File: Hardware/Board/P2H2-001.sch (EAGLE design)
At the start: 18 parts, among them K1 G5V1, T1 2SC1815

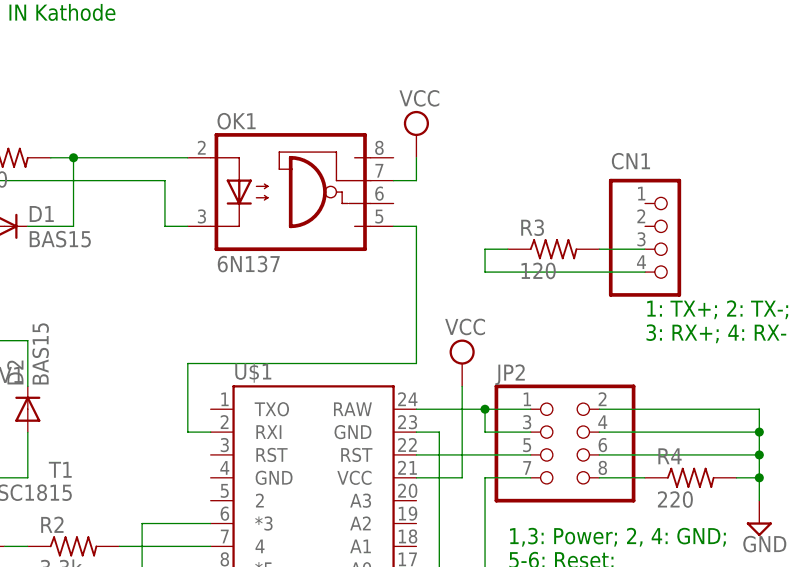
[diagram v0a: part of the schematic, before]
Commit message: Fixed connection error of MIDI IN.
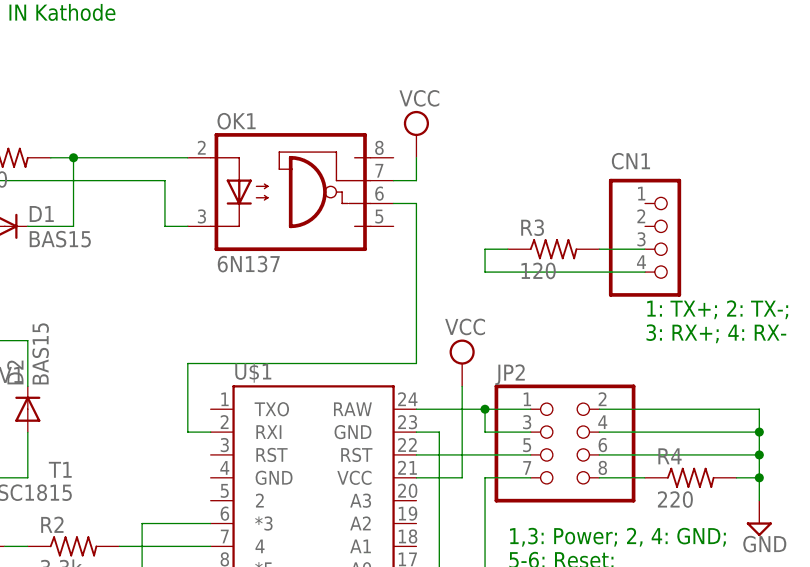
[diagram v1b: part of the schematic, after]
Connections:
- net N$12: now also OK1.VO; no longer OK1.GND
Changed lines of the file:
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@@
 <net name="N$12" class="0">
 <segment>
-<pinref part="OK1" gate="A" pin="GND"/>
-<wire x1="81.28" y1="66.04" x2="83.82" y2="66.04" width="0.1524" layer="91"/>
-<wire x1="83.82" y1="66.04" x2="83.82" y2="50.8" width="0.1524" layer="91"/>
+<wire x1="83.82" y1="68.58" x2="83.82" y2="50.8" width="0.1524" layer="91"/>
 <wire x1="83.82" y1="50.8" x2="58.42" y2="50.8" width="0.1524" layer="91"/>
 <wire x1="58.42" y1="50.8" x2="58.42" y2="43.18" width="0.1524" layer="91"/>
 <pinref part="U$1" gate="G$1" pin="RXI"/>
 <wire x1="58.42" y1="43.18" x2="60.96" y2="43.18" width="0.1524" layer="91"/>
+<pinref part="OK1" gate="A" pin="VO"/>
+<wire x1="81.28" y1="68.58" x2="83.82" y2="68.58" width="0.1524" layer="91"/>
 </segment>
 </net>

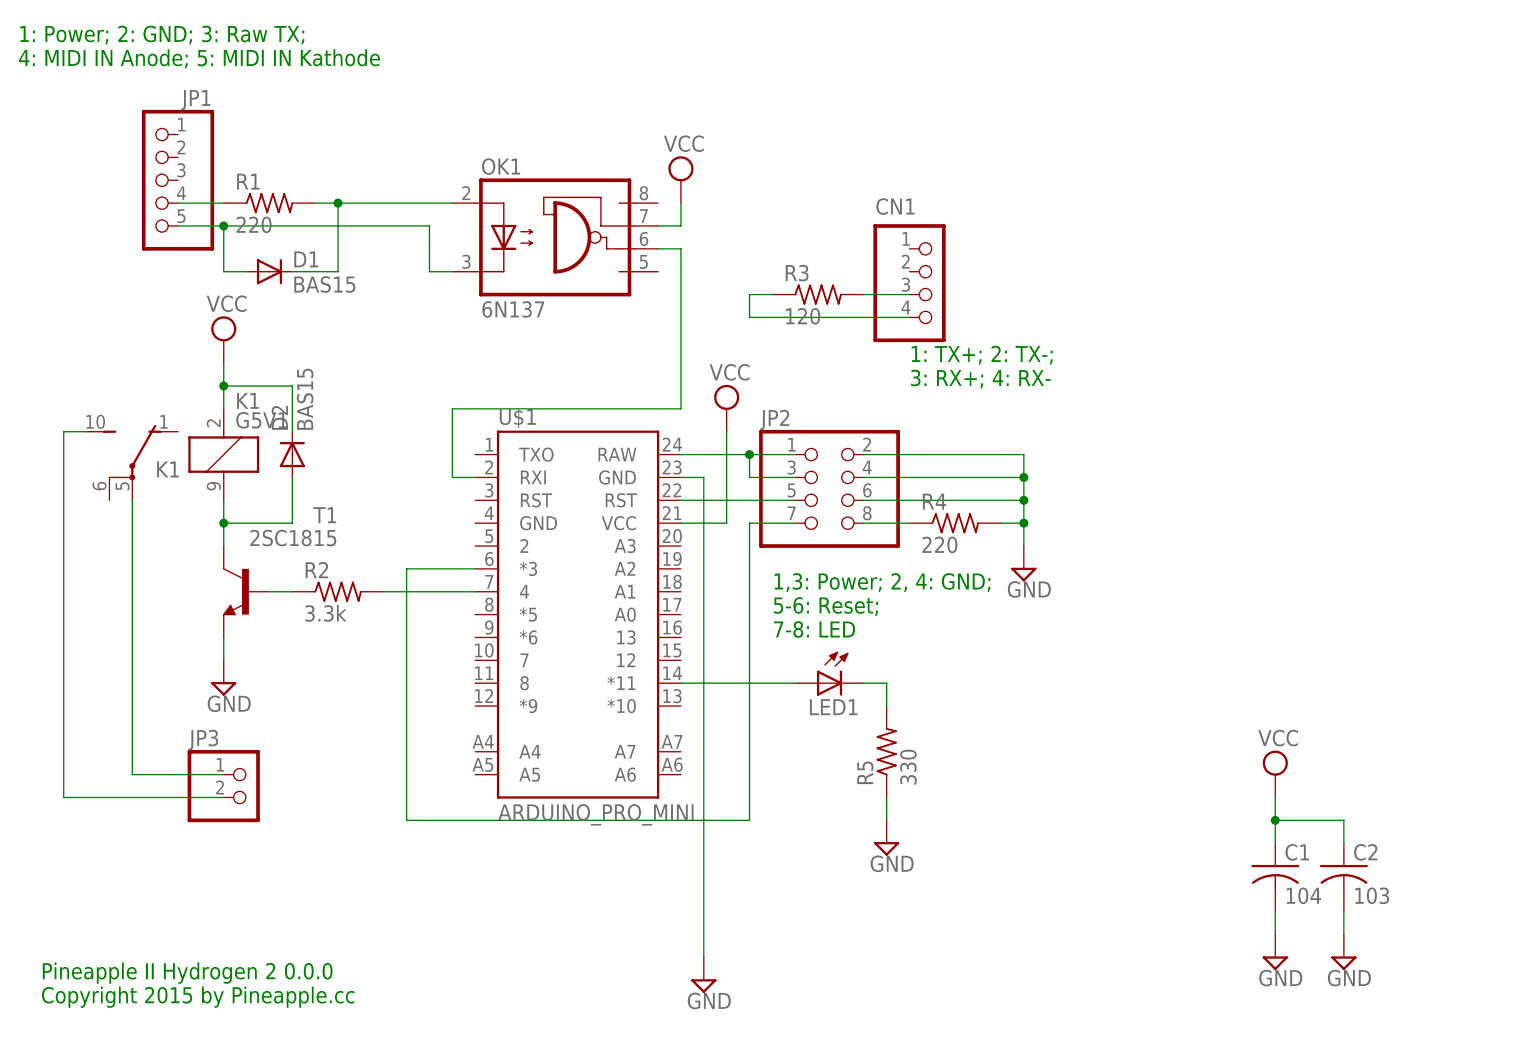
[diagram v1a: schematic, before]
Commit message: Adopted to Relayport.
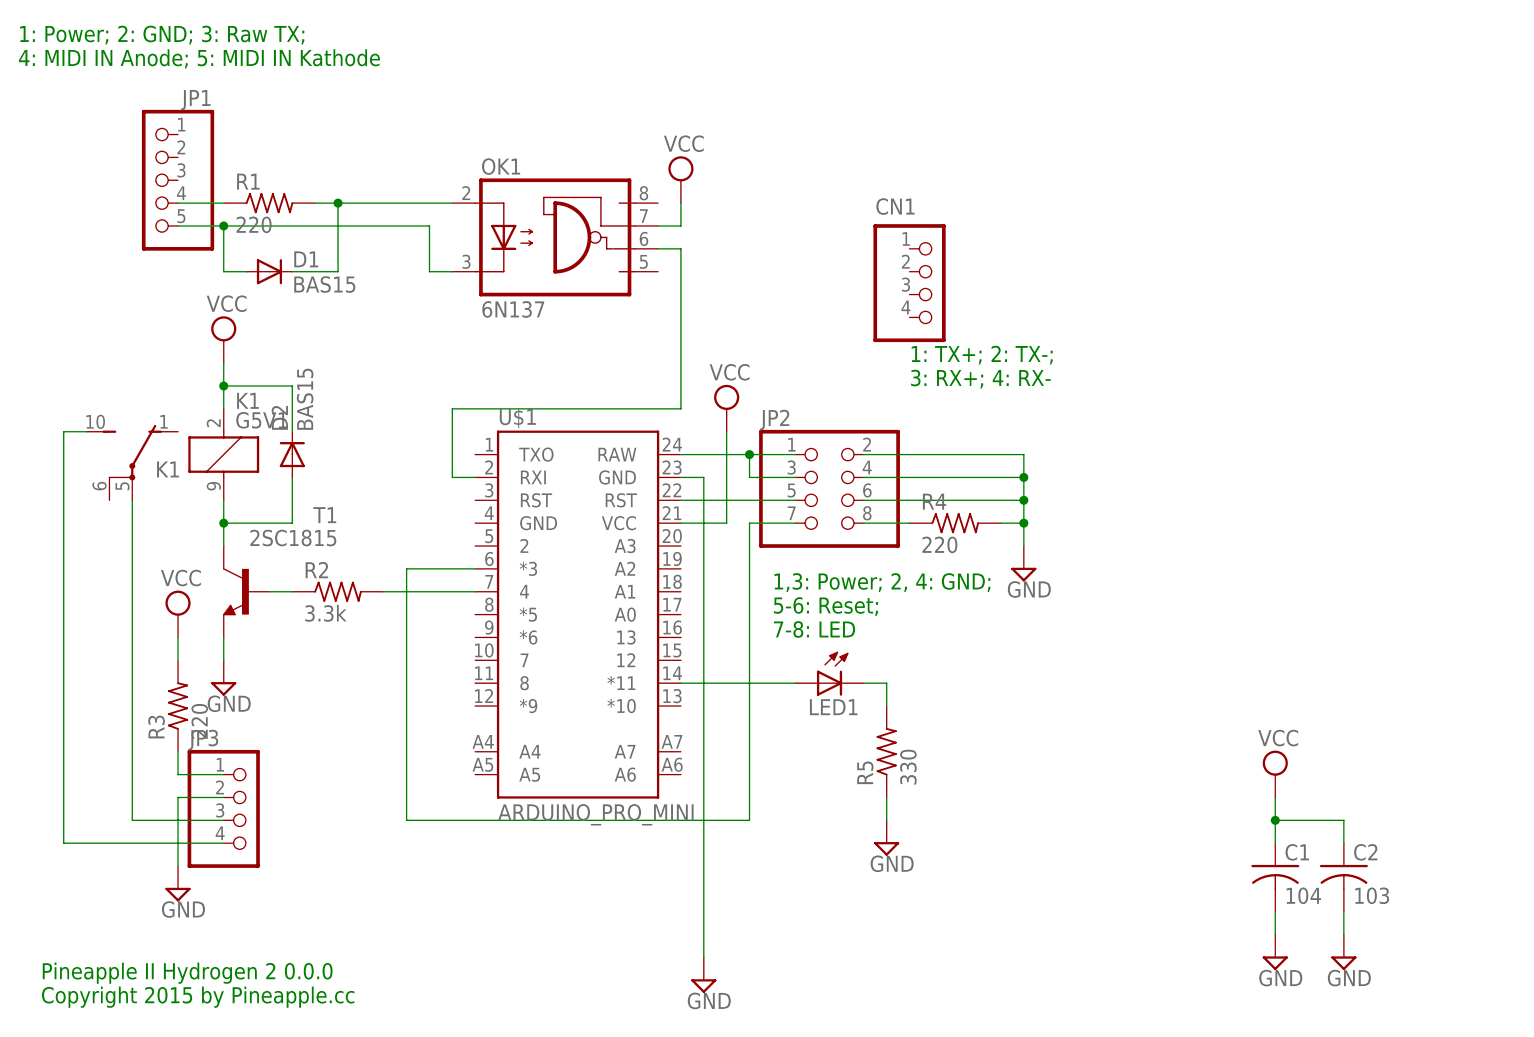
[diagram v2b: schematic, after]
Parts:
- JP3: device pinhead:PINHD-1X2 -> pinhead:PINHD-1X4
- R3: value 120 -> 220
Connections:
- removed net N$1: CN1.3, R3.2
- removed net N$2: CN1.4, R3.1
- new net N$10: JP3.1, R3.1
- net GND: now also JP3.2
- net N$18: now also JP3.3; no longer JP3.1
- net N$19: now also JP3.4; no longer JP3.2
- net VCC: now also R3.2
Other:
- moved on the sheet: R3
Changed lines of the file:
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@@
 <part name="SUPPLY6" library="supply2" deviceset="GND" device=""/>
 <part name="R4" library="resistor" deviceset="R-US_" device="0204/5" value="220"/>
-<part name="R3" library="resistor" deviceset="R-US_" device="0204/5" value="120"/>
+<part name="R3" library="resistor" deviceset="R-US_" device="0204/5" value="220"/>
 <part name="CN1" library="jst-ph" deviceset="B4B-PH-*" device="K-S"/>
 <part name="U$1" library="SparkFun-Boards" deviceset="ARDUINO_PRO_MINI" device=""/>
@@
 <part name="SUPPLY3" library="supply2" deviceset="VCC" device=""/>
 <part name="R2" library="resistor" deviceset="R-US_" device="0204/5" value="3.3k"/>
-<part name="JP3" library="pinhead" deviceset="PINHD-1X2" device=""/>
+<part name="JP3" library="pinhead" deviceset="PINHD-1X4" device=""/>
+<part name="SUPPLY10" library="supply2" deviceset="GND" device=""/>
+<part name="SUPPLY12" library="supply2" deviceset="VCC" device=""/>
 </parts>
 <sheets>
@@
 <instance part="SUPPLY6" gate="GND" x="121.92" y="33.02"/>
 <instance part="R4" gate="G$1" x="114.3" y="38.1"/>
-<instance part="R3" gate="G$1" x="99.06" y="63.5"/>
+<instance part="R3" gate="G$1" x="27.94" y="17.78" rot="R90"/>
 <instance part="CN1" gate="G$1" x="109.22" y="66.04"/>
 <instance part="U$1" gate="G$1" x="71.12" y="30.48"/>
@@
 <instance part="SUPPLY3" gate="G$1" x="33.02" y="58.42"/>
 <instance part="R2" gate="G$1" x="45.72" y="30.48"/>
-<instance part="JP3" gate="G$1" x="35.56" y="7.62"/>
+<instance part="JP3" gate="A" x="35.56" y="5.08"/>
+<instance part="SUPPLY10" gate="GND" x="27.94" y="-2.54"/>
+<instance part="SUPPLY12" gate="G$1" x="27.94" y="27.94"/>
 </instances>
 <busses>
@@
 <wire x1="106.68" y1="5.08" x2="106.68" y2="7.62" width="0.1524" layer="91"/>
 </segment>
+<segment>
+<pinref part="JP3" gate="A" pin="2"/>
+<pinref part="SUPPLY10" gate="GND" pin="GND"/>
+<wire x1="33.02" y1="7.62" x2="27.94" y2="7.62" width="0.1524" layer="91"/>
+<wire x1="27.94" y1="7.62" x2="27.94" y2="0" width="0.1524" layer="91"/>
+</segment>
 </net>
 <net name="VCC" class="0">
@@
 <wire x1="40.64" y1="53.34" x2="33.02" y2="53.34" width="0.1524" layer="91"/>
 <junction x="33.02" y="53.34"/>
+</segment>
+<segment>
+<pinref part="SUPPLY12" gate="G$1" pin="VCC"/>
+<wire x1="27.94" y1="25.4" x2="27.94" y2="22.86" width="0.1524" layer="91"/>
+<pinref part="R3" gate="G$1" pin="2"/>
 </segment>
 </net>
@@
 <segment>
 <pinref part="K1" gate="2" pin="P"/>
-<wire x1="22.86" y1="10.16" x2="22.86" y2="40.64" width="0.1524" layer="91"/>
-<pinref part="JP3" gate="G$1" pin="1"/>
-<wire x1="22.86" y1="10.16" x2="33.02" y2="10.16" width="0.1524" layer="91"/>
+<wire x1="22.86" y1="5.08" x2="22.86" y2="40.64" width="0.1524" layer="91"/>
+<pinref part="JP3" gate="A" pin="3"/>
+<wire x1="33.02" y1="5.08" x2="22.86" y2="5.08" width="0.1524" layer="91"/>
 </segment>
 </net>
@@
 <pinref part="K1" gate="2" pin="S"/>
 <wire x1="17.78" y1="48.26" x2="15.24" y2="48.26" width="0.1524" layer="91"/>
-<wire x1="15.24" y1="48.26" x2="15.24" y2="7.62" width="0.1524" layer="91"/>
-<pinref part="JP3" gate="G$1" pin="2"/>
-<wire x1="15.24" y1="7.62" x2="33.02" y2="7.62" width="0.1524" layer="91"/>
+<wire x1="15.24" y1="48.26" x2="15.24" y2="2.54" width="0.1524" layer="91"/>
+<pinref part="JP3" gate="A" pin="4"/>
+<wire x1="33.02" y1="2.54" x2="15.24" y2="2.54" width="0.1524" layer="91"/>
 </segment>
 </net>
@@
 </segment>
 </net>
-<net name="N$1" class="0">
-<segment>
-<pinref part="CN1" gate="G$1" pin="3"/>
-<pinref part="R3" gate="G$1" pin="2"/>
-<wire x1="109.22" y1="63.5" x2="104.14" y2="63.5" width="0.1524" layer="91"/>
-</segment>
-</net>
-<net name="N$2" class="0">
-<segment>
-<pinref part="CN1" gate="G$1" pin="4"/>
-<wire x1="109.22" y1="60.96" x2="91.44" y2="60.96" width="0.1524" layer="91"/>
-<wire x1="91.44" y1="60.96" x2="91.44" y2="63.5" width="0.1524" layer="91"/>
-<pinref part="R3" gate="G$1" pin="1"/>
-<wire x1="91.44" y1="63.5" x2="93.98" y2="63.5" width="0.1524" layer="91"/>
-</segment>
-</net>
 <net name="N$13" class="0">
 <segment>
@@
 </segment>
 </net>
+<net name="N$10" class="0">
+<segment>
+<wire x1="27.94" y1="12.7" x2="27.94" y2="10.16" width="0.1524" layer="91"/>
+<pinref part="JP3" gate="A" pin="1"/>
+<wire x1="27.94" y1="10.16" x2="33.02" y2="10.16" width="0.1524" layer="91"/>
+<pinref part="R3" gate="G$1" pin="1"/>
+</segment>
+</net>

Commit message: Changed layout of ZeroVoltage.
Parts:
- JP2: device pinhead:PINHD-2X4 -> pinhead:PINHD-1X4
- JP3: device pinhead:PINHD-1X4 -> pinhead:PINHD-2X4
- R2: value 3.3k -> 220
- R3: value 220 -> 3.3k
- R4: value 220 -> 330
- R5: value 330 -> 150
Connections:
- removed net N$14: R2.2, U$1.4
- new net N$1: R3.2, U$1.7
- net GND: now also JP3.4, JP3.6, R4.1, R5.2; no longer JP2.4, JP2.6, R4.2, R5.1
- net N$10: now also JP2.1, R1.1; no longer JP3.1, R3.1
- net N$13: now also R3.1; no longer R2.1
- net N$17: now also R4.2; no longer R5.2
- net N$18: now also JP2.3; no longer JP3.3
- net N$19: now also JP2.4; no longer JP3.4
- net N$3: now also R2.1; no longer R1.1
- net N$4: now also R2.2; no longer R1.2
- net N$5: now also JP3.8, R5.1; no longer JP2.8, R4.1
- net N$6: now also JP3.5; no longer JP2.5
- net N$8: now also JP3.7; no longer JP2.7
- net N$9: now also JP3.1, JP3.3; no longer JP2.1, JP2.3
- net VCC: now also R1.2; no longer R3.2
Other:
- moved on the sheet: R1, R2, R3, R4, R5

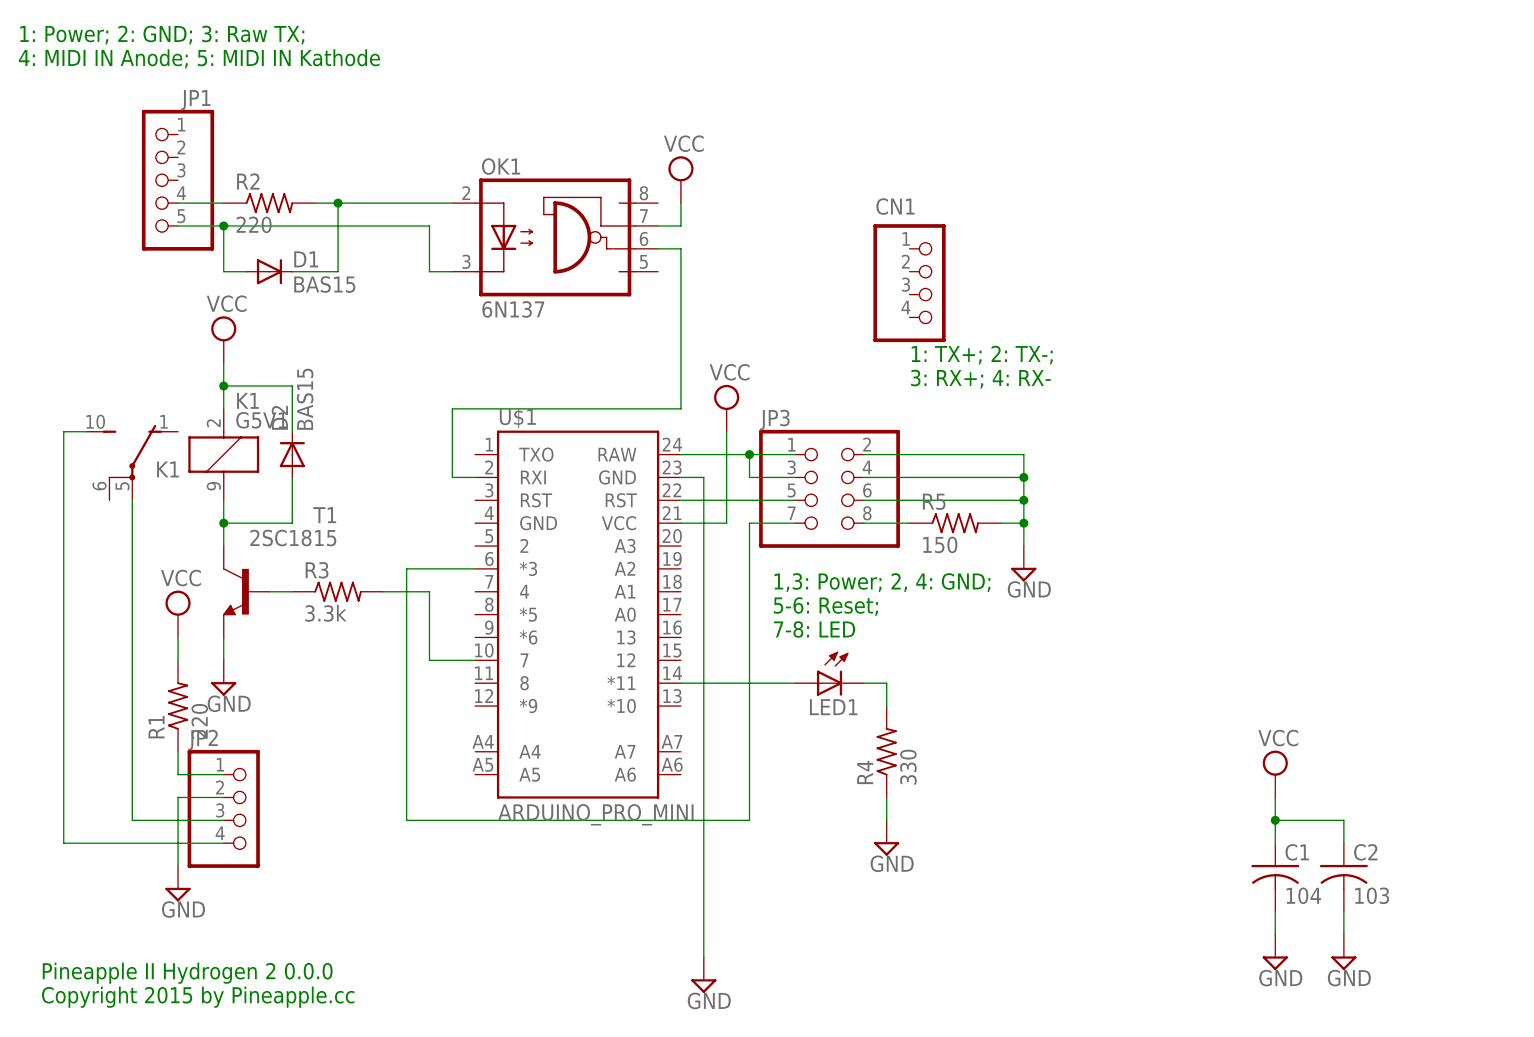
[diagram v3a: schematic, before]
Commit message: Merged H2 and H3.
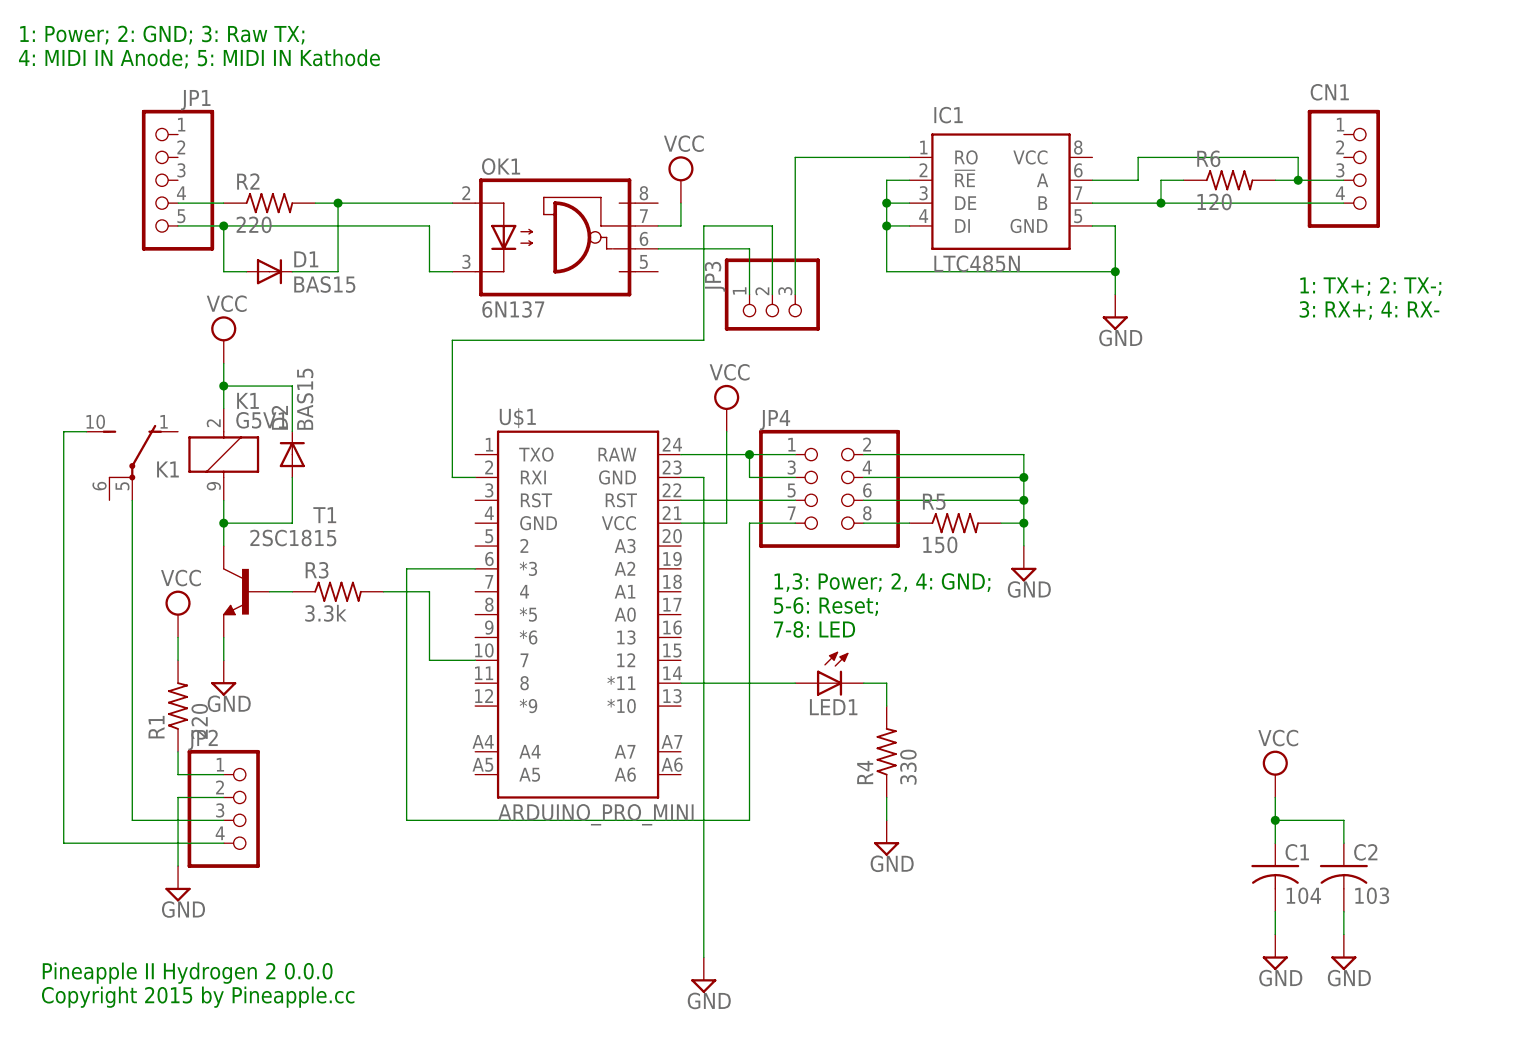
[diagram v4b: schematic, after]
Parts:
- added IC1: LTC485N, linear-technology:LTC485N
- added JP4: (no value), pinhead:PINHD-2X4
- added R6: 120, resistor:R-US_0204/5
- JP3: device pinhead:PINHD-2X4 -> pinhead:PINHD-1X3
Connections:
- new net N$11: CN1.4, IC1.B, R6.1
- new net N$14: IC1.RO, JP3.3
- new net N$2: CN1.3, IC1.A, R6.2
- new net N$20: JP3.2, U$1.RXI
- net GND: now also IC1.!RE, IC1.DE, IC1.DI, IC1.GND, JP4.2, JP4.4, JP4.6; no longer JP3.2, JP3.4, JP3.6
- net N$12: now also JP3.1; no longer U$1.RXI
- net N$5: now also JP4.8; no longer JP3.8
- net N$6: now also JP4.5; no longer JP3.5
- net N$8: now also JP4.7; no longer JP3.7
- net N$9: now also JP4.1, JP4.3; no longer JP3.1, JP3.3
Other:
- moved on the sheet: CN1
